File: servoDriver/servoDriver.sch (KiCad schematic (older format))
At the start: 19 parts, among them J1 Conn_01x04_Male, J2 Conn_01x04_Male, J3 Conn_01x03_Male, J4 Conn_01x03_Male, J5 Conn_01x03_Male, J6 SWD, U1 STM32F042F6Px, U2 AP131-33, U3 TCAN330, Y1 8MHz

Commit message: Version 2 PCB?
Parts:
- J6: footprint Connector_PinHeader_1.00mm:PinHeader_1x04_P1.00mm_Vertical -> Connector_PinHeader_1.27mm:PinHeader_1x04_P1.27mm_Vertical
- JP1, JP2: footprint Jumper:SolderJumper-2_P1.3mm_Open_Pad1.0x1.5mm -> servoDriver:SolderJumper-2_P1.3mm_Open_RoundedPad1.0x1.5mm
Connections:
- wire segments 127 -> 129
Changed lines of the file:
@@
 EESchema Schematic File Version 4
+LIBS:servoDriver-cache
 EELAYER 30 0
 EELAYER END
@@
 F 0 "J6" H 7722 2332 50  0000 R CNN
 F 1 "SWD" H 7722 2423 50  0000 R CNN
-F 2 "Connector_PinHeader_1.00mm:PinHeader_1x04_P1.00mm_Vertical" H 7750 2450 50  0001 C CNN
+F 2 "Connector_PinHeader_1.27mm:PinHeader_1x04_P1.27mm_Vertical" H 7750 2450 50  0001 C CNN
 F 3 "~" H 7750 2450 50  0001 C CNN
 	1    7750 2450
@@
 	4350 3850 4350 4300
 Wire Wire Line
-	4350 4300 5700 4300
+	4350 4300 5300 4300
 Connection ~ 4350 3850
 Connection ~ 5700 4300
@@
 F 0 "JP1" H 5850 6055 50  0000 C CNN
 F 1 "SolderJumper_2_Open" H 5850 5964 50  0000 C CNN
-F 2 "Jumper:SolderJumper-2_P1.3mm_Open_Pad1.0x1.5mm" H 5850 5850 50  0001 C CNN
+F 2 "servoDriver:SolderJumper-2_P1.3mm_Open_RoundedPad1.0x1.5mm" H 5850 5850 50  0001 C CNN
 F 3 "~" H 5850 5850 50  0001 C CNN
 	1    5850 5850
@@
 F 0 "JP2" H 5850 6355 50  0000 C CNN
 F 1 "SolderJumper_2_Open" H 5850 6264 50  0000 C CNN
-F 2 "Jumper:SolderJumper-2_P1.3mm_Open_Pad1.0x1.5mm" H 5850 6150 50  0001 C CNN
+F 2 "servoDriver:SolderJumper-2_P1.3mm_Open_RoundedPad1.0x1.5mm" H 5850 6150 50  0001 C CNN
 F 3 "~" H 5850 6150 50  0001 C CNN
 	1    5850 6150
@@
 Wire Wire Line
 	6550 5350 6950 5350
+Wire Wire Line
+	5300 4050 5300 4300
+Connection ~ 5300 4300
+Wire Wire Line
+	5300 4300 5700 4300
 $EndSCHEMATC

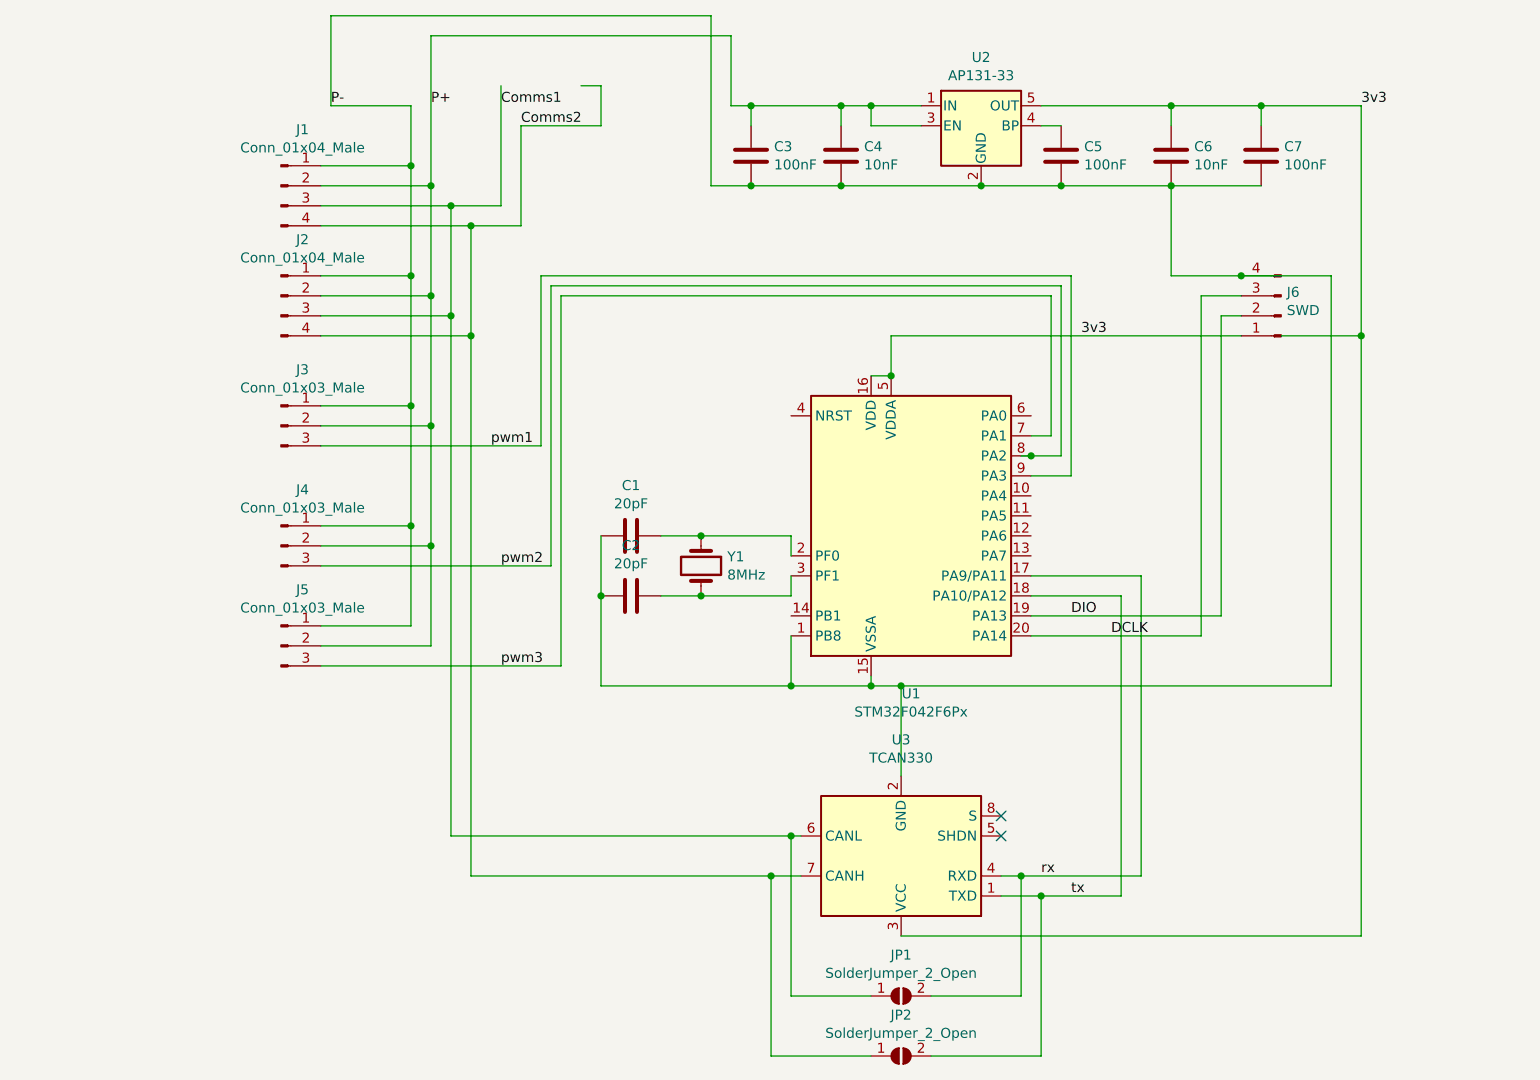
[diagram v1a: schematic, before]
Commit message: PCB updates  * V3  * Added extra channel  * Using closely spaced pins.
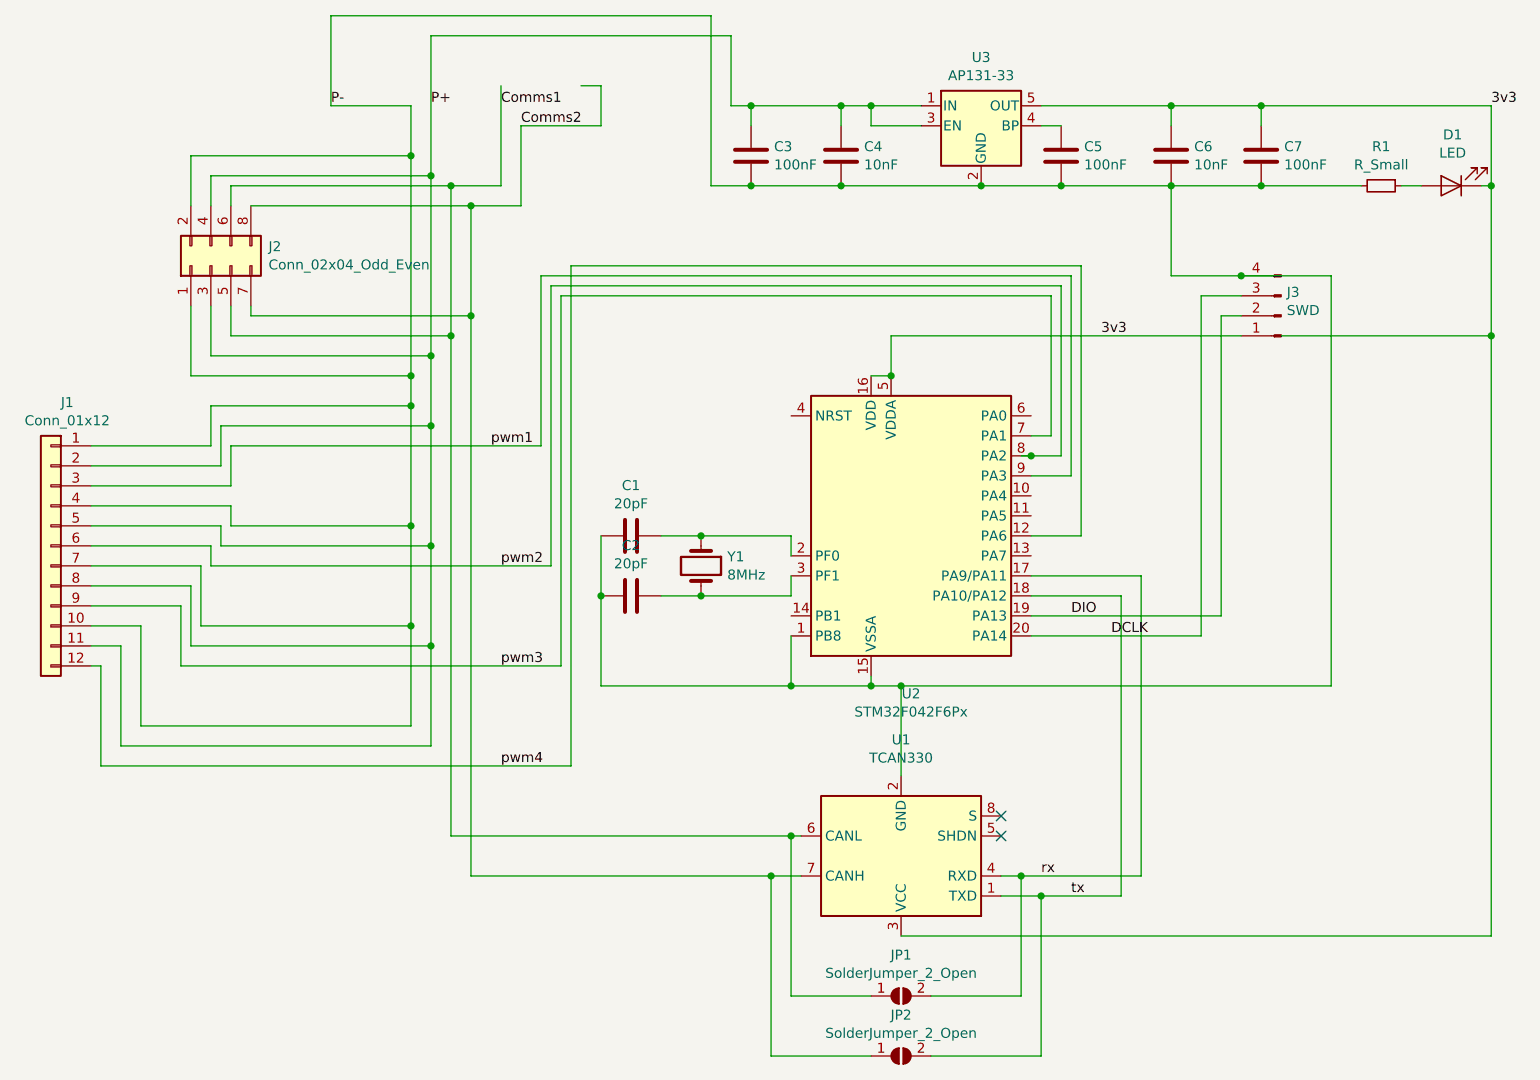
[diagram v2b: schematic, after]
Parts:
- removed J1, J2: Conn_01x04_Male, Connector_PinHeader_2.54mm:PinHeader_1x04_P2.54mm_Vertical, symbol Connector:Conn_01x04_Male
- removed J3, J4, J5: Conn_01x03_Male, Connector_PinHeader_2.54mm:PinHeader_1x03_P2.54mm_Vertical, symbol Connector:Conn_01x03_Male
- added D1: LED, LED_SMD:LED_0603_1608Metric, symbol Device:LED
- added J1: Conn_01x12, servoDriver:PinHeader_3x04_P2.54mm_Vertical, symbol Connector_Generic:Conn_01x12
- added J2: Conn_02x04_Odd_Even, symbol Connector_Generic:Conn_02x04_Odd_Even
- added R1: R_Small, Resistor_SMD:R_0603_1608Metric, symbol Device:R_Small
- renumbered J6 to J3, U3 to U1, U1 to U2, U2 to U3
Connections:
- net labels added: pwm4
- wire segments 129 -> 174
